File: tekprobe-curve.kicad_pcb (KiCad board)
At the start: 4 copper layers, 44 x 21.8 mm, 30 parts, among them J1 Probe, J2 TekProbe_BNC, J3 TekProbe_Header, J4 Pigtail_BNC, U1 TL074, U2 24C02

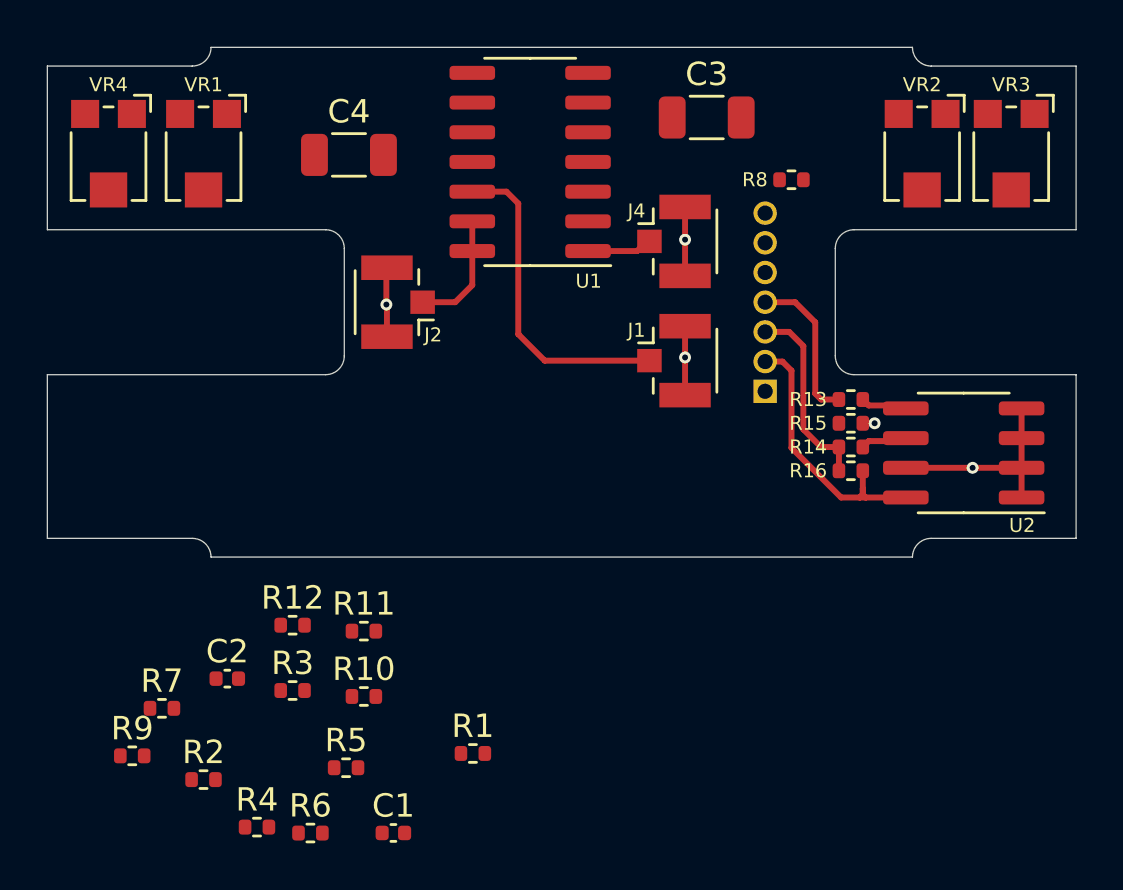
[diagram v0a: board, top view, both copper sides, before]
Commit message: Convert to KiCad 6.
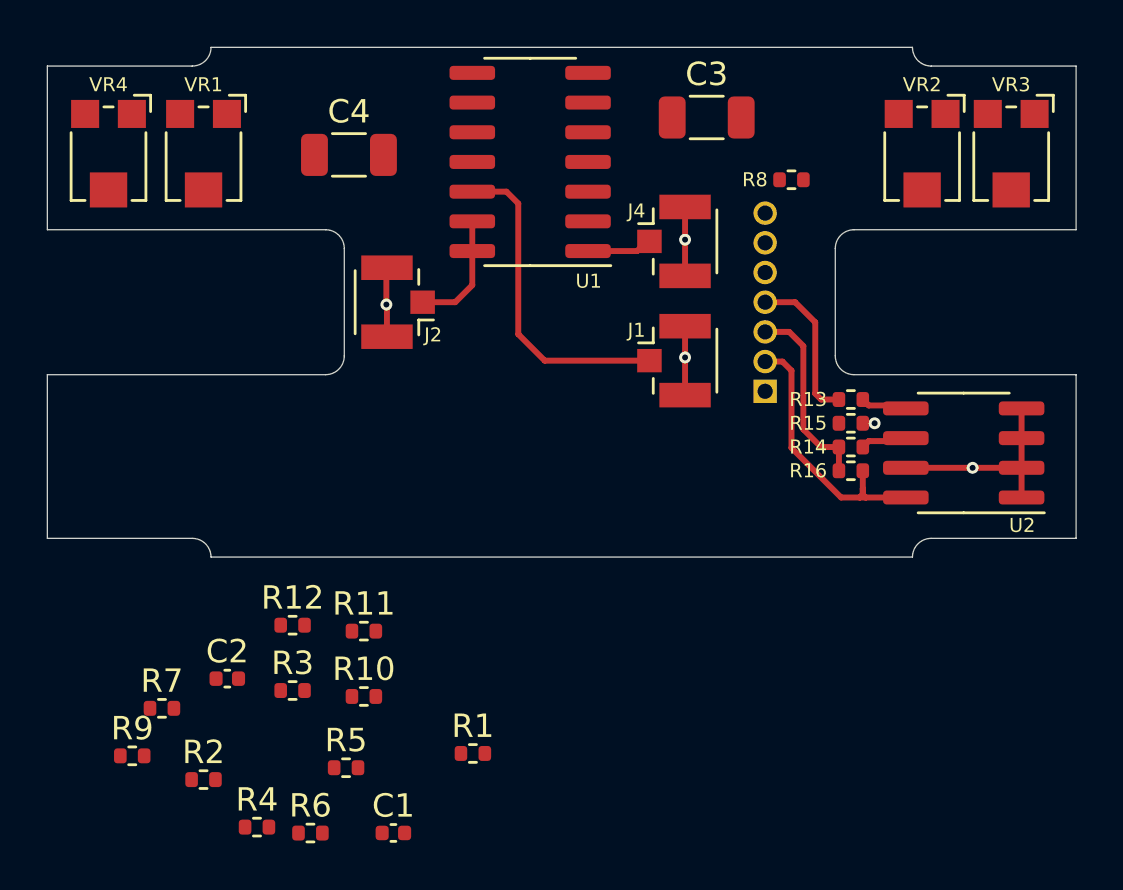
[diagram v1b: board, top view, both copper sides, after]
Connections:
- J3 pad 6: Net-(J3-Pad6) -> unconnected-(J3-Pad6)
- J3 pad 7: Net-(J3-Pad7) -> unconnected-(J3-Pad7)
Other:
- net class Default removed
- net class Power removed
